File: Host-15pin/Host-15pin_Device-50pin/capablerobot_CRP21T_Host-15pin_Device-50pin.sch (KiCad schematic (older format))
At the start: 2 parts, among them J1 WE_686715100001_FLEX, J2 WE_687650100002_FLEX

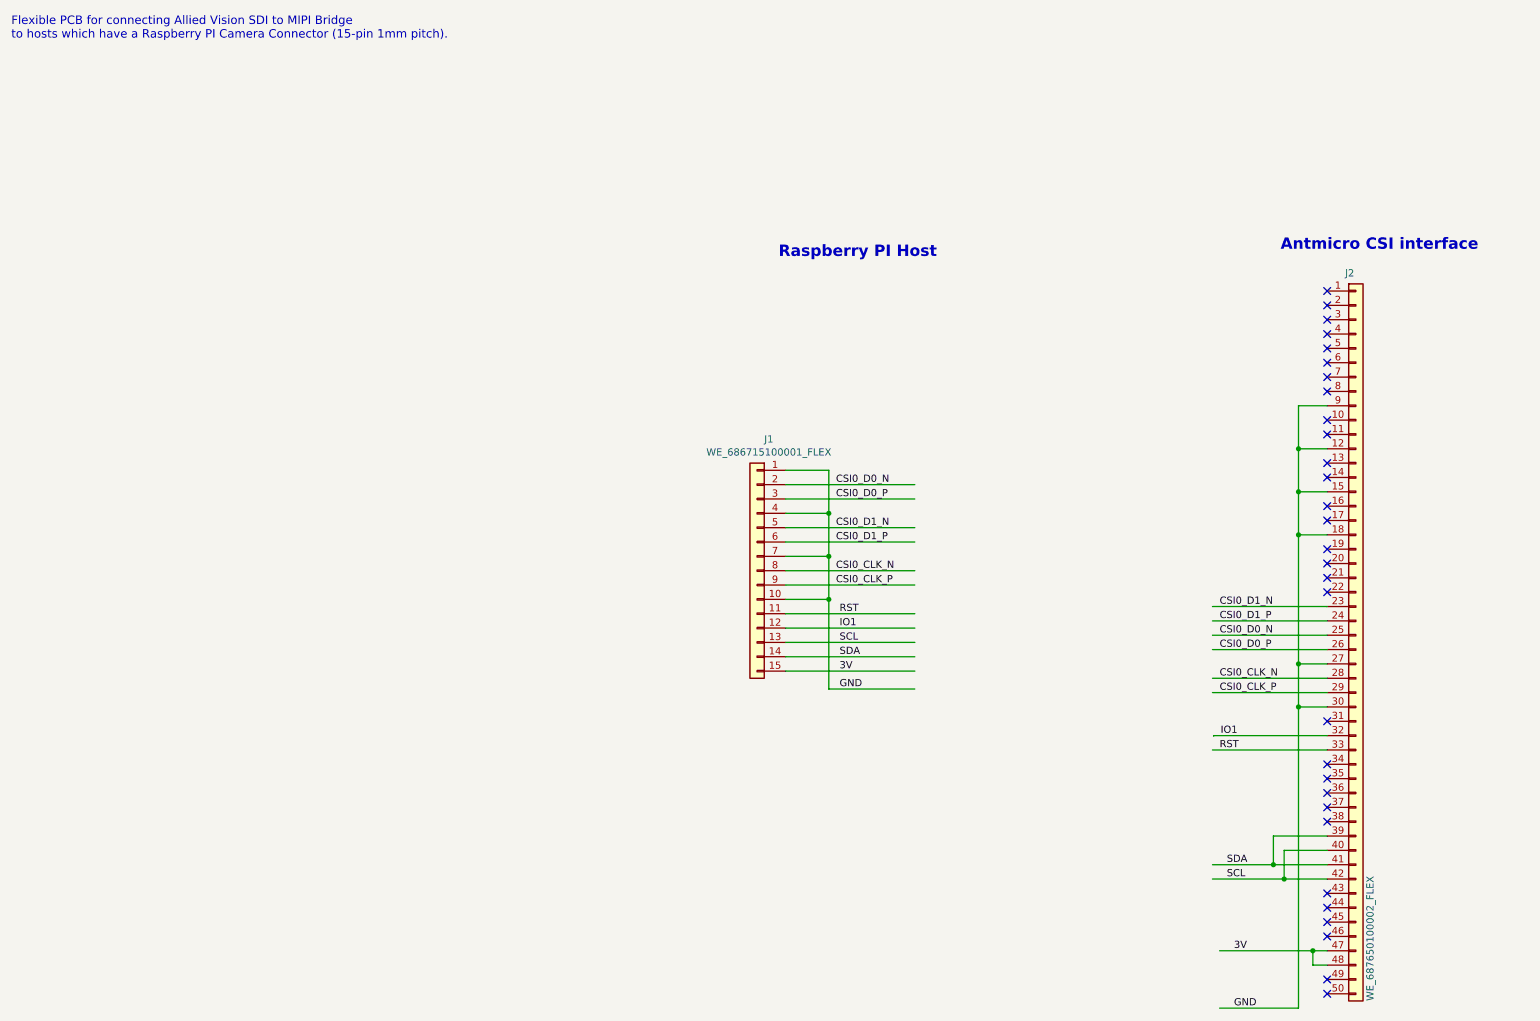
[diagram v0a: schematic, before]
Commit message: Change 22 pin to 4 lane interface and change 15 pin and 22 pin to alternate MIPI interface
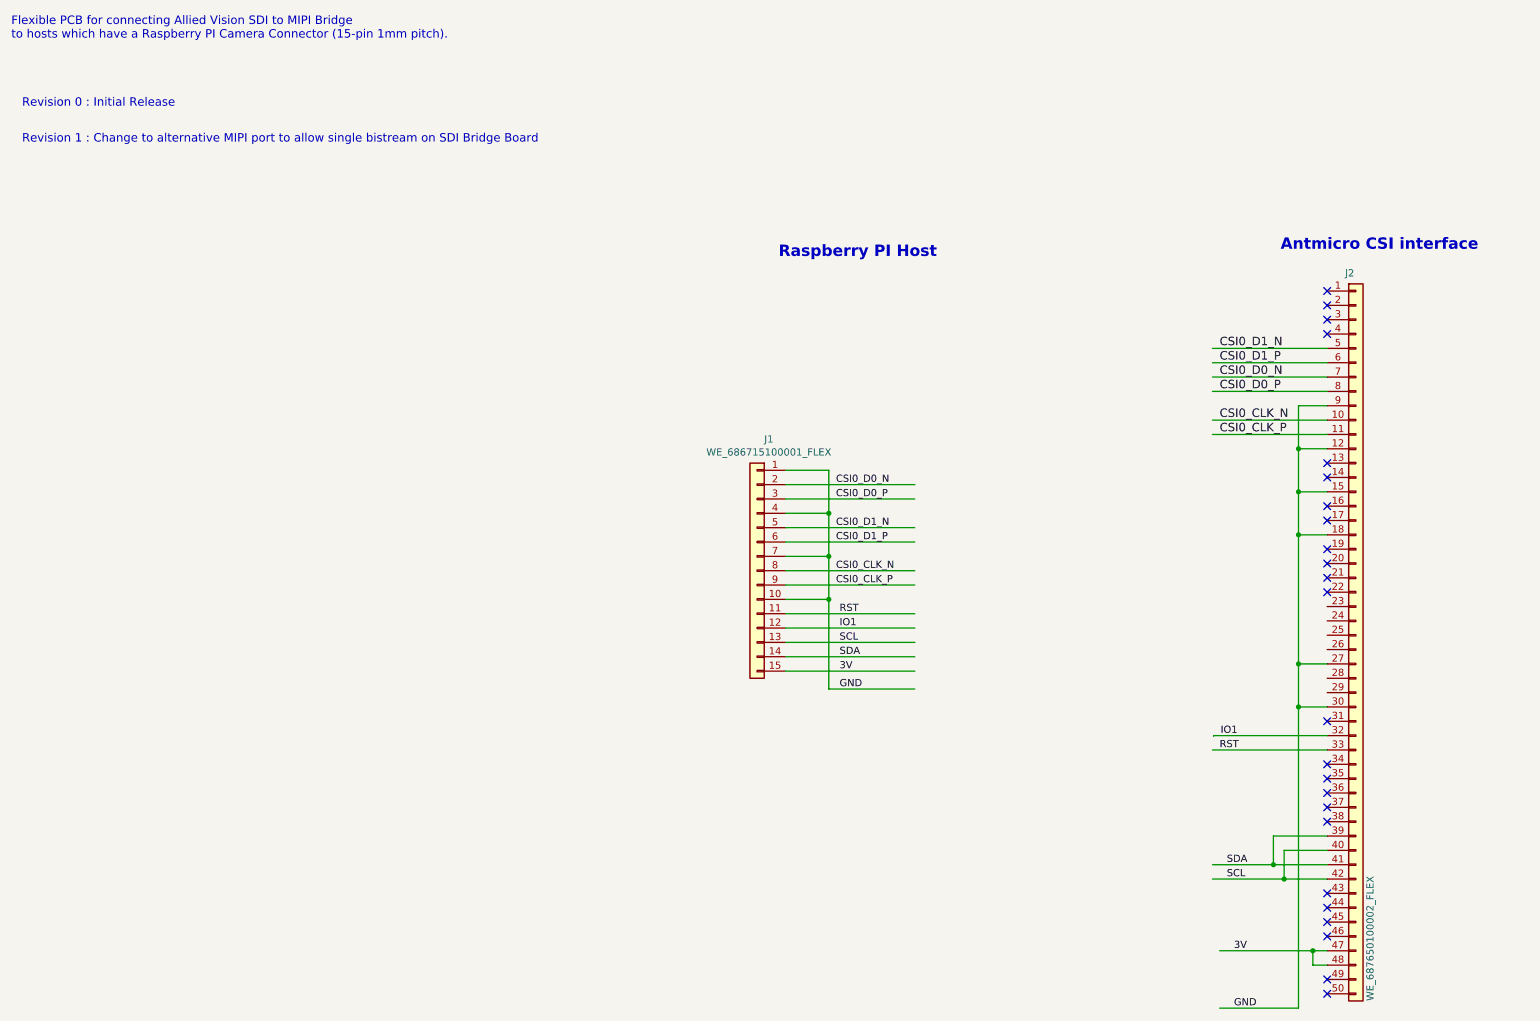
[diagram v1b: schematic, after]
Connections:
- no-connect marks 30 -> 24
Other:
- note added: "Revision 0 : Initial Release"
- note added: "Revision 1 : Change to alternative MIPI port to allow single bistream on SDI Bridge Board"
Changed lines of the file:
@@
 NoConn ~ 10100 3475
 NoConn ~ 10100 3575
-NoConn ~ 10100 3675
-NoConn ~ 10100 3775
-NoConn ~ 10100 3875
-NoConn ~ 10100 3975
-NoConn ~ 10100 4175
-NoConn ~ 10100 4275
 NoConn ~ 10100 4475
 NoConn ~ 10100 4575
@@
 Text Label 9400 7375 0    50   ~ 0
 SCL
-Text Label 9350 5475 0    50   ~ 0
-CSI0_D1_N
-Text Label 9350 5575 0    50   ~ 0
-CSI0_D1_P
-Text Label 9350 5675 0    50   ~ 0
-CSI0_D0_N
-Text Label 9350 5775 0    50   ~ 0
-CSI0_D0_P
-Text Label 9350 5975 0    50   ~ 0
-CSI0_CLK_N
-Text Label 9350 6075 0    50   ~ 0
-CSI0_CLK_P
-Wire Wire Line
-	10100 6075 9300 6075
-Wire Wire Line
-	10100 5975 9300 5975
-Wire Wire Line
-	10100 5775 9300 5775
-Wire Wire Line
-	10100 5675 9300 5675
-Wire Wire Line
-	10100 5575 9300 5575
-Wire Wire Line
-	10100 5475 9300 5475
 Wire Wire Line
 	10100 7375 9800 7375
@@
 Wire Wire Line
 	9725 7275 9300 7275
+Text Notes 1000 2000 0    59   ~ 0
+Revision 0 : Initial Release
+Text Notes 1000 2250 0    59   ~ 0
+Revision 1 : Change to alternative MIPI port to allow single bistream on SDI Bridge Board
+Wire Wire Line
+	10100 4275 9300 4275
+Wire Wire Line
+	10100 4175 9300 4175
+Wire Wire Line
+	10100 3975 9300 3975
+Wire Wire Line
+	10100 3875 9300 3875
+Wire Wire Line
+	10100 3775 9300 3775
+Wire Wire Line
+	10100 3675 9300 3675
+Text Label 9350 4275 0    59   ~ 0
+CSI0_CLK_P
+Text Label 9350 4175 0    59   ~ 0
+CSI0_CLK_N
+Text Label 9350 3975 0    59   ~ 0
+CSI0_D0_P
+Text Label 9350 3875 0    59   ~ 0
+CSI0_D0_N
+Text Label 9350 3775 0    59   ~ 0
+CSI0_D1_P
+Text Label 9350 3675 0    59   ~ 0
+CSI0_D1_N
 $EndSCHEMATC
